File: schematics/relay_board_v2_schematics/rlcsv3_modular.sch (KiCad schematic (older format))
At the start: 37 parts, among them J1 Programming Header, P1 ACT_PWR, P3 ACTUATOR, Q1 MMBF170, Q2 MMBF170, SW1 SW_DIP_x04, U1 SPST_POWER_RELAY, U2 PIC16F1826-ISO, U3 dpdt_relay, U4 INA180A1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

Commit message: Add footprint to library
Signed-off-by: AIDAN HA <qbha@edu.uwaterloo.ca>
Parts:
- C1: footprint (none) -> Capacitors_SMD:C_0805_HandSoldering
- J1: footprint (none) -> rlcs:PinHeader_5x2.54_SMD_90deg_952-3198-1-ND
- R1, R13, R2, R3, R4: footprint (none) -> Resistors_SMD:R_0805_HandSoldering
- SW1: footprint (none) -> rlcs:DIP_SWITCH_4X2
- U2: footprint (none) -> rlcs:PIC16F1826-ISO
- U5: footprint (none) -> rlcs:2.54mm_pitch_1.3mm_hole_1x3_socket
- U6: footprint TO_SOT_Packages_SMD:SOT-23-5_HandSoldering -> rlcs:DCDC-Conv_IV1215SA
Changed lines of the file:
@@
 F 0 "U5" H 4938 1375 60  0000 L CNN
 F 1 "CONN_01x05" H 4938 1269 60  0000 L CNN
-F 2 "" H 4850 1600 60  0001 C CNN
+F 2 "rlcs:2.54mm_pitch_1.3mm_hole_1x3_socket" H 4850 1600 60  0001 C CNN
 F 3 "" H 4850 1600 60  0001 C CNN
 	1    4850 1500
@@
 F 0 "J1" H 1628 1226 50  0000 L CNN
 F 1 "Programming Header" H 1628 1135 50  0000 L CNN
-F 2 "" H 1600 1200 50  0001 C CNN
+F 2 "rlcs:PinHeader_5x2.54_SMD_90deg_952-3198-1-ND" H 1600 1200 50  0001 C CNN
 F 3 "~" H 1600 1200 50  0001 C CNN
 	1    1600 1200
@@
 F 0 "R1" H 2170 2496 50  0000 L CNN
 F 1 "10k" H 2170 2405 50  0000 L CNN
-F 2 "" V 2030 2450 50  0001 C CNN
+F 2 "Resistors_SMD:R_0805_HandSoldering" V 2030 2450 50  0001 C CNN
 F 3 "~" H 2100 2450 50  0001 C CNN
 	1    2100 2450
@@
 F 0 "SW1" H 1800 3267 50  0000 C CNN
 F 1 "SW_DIP_x04" H 1800 3176 50  0000 C CNN
-F 2 "" H 1800 2800 50  0001 C CNN
+F 2 "rlcs:DIP_SWITCH_4X2" H 1800 2800 50  0001 C CNN
 F 3 "~" H 1800 2800 50  0001 C CNN
 	1    1800 2800
@@
 F 0 "R3" H 3070 2496 50  0000 L CNN
 F 1 "10k" H 3070 2405 50  0000 L CNN
-F 2 "" V 2930 2450 50  0001 C CNN
+F 2 "Resistors_SMD:R_0805_HandSoldering" V 2930 2450 50  0001 C CNN
 F 3 "~" H 3000 2450 50  0001 C CNN
 	1    3000 2450
@@
 F 0 "R2" H 2670 2496 50  0000 L CNN
 F 1 "10k" H 2670 2405 50  0000 L CNN
-F 2 "" V 2530 2450 50  0001 C CNN
+F 2 "Resistors_SMD:R_0805_HandSoldering" V 2530 2450 50  0001 C CNN
 F 3 "~" H 2600 2450 50  0001 C CNN
 	1    2600 2450
@@
 F 0 "R4" H 3470 2496 50  0000 L CNN
 F 1 "10k" H 3470 2405 50  0000 L CNN
-F 2 "" V 3330 2450 50  0001 C CNN
+F 2 "Resistors_SMD:R_0805_HandSoldering" V 3330 2450 50  0001 C CNN
 F 3 "~" H 3400 2450 50  0001 C CNN
 	1    3400 2450
@@
 F 0 "R13" H 5130 2496 50  0000 L CNN
 F 1 "10K" H 5130 2405 50  0000 L CNN
-F 2 "" V 4990 2450 50  0001 C CNN
+F 2 "Resistors_SMD:R_0805_HandSoldering" V 4990 2450 50  0001 C CNN
 F 3 "~" H 5060 2450 50  0001 C CNN
 	1    5060 2450
@@
 F 0 "C1" V 7913 2546 50  0000 L CNN
 F 1 "22uF" V 7835 2455 50  0000 L CNN
-F 2 "" H 7758 2350 50  0001 C CNN
+F 2 "Capacitors_SMD:C_0805_HandSoldering" H 7758 2350 50  0001 C CNN
 F 3 "~" H 7720 2500 50  0001 C CNN
 	1    7720 2500
@@
 F 0 "U2" H 6200 3087 60  0000 C CNN
 F 1 "PIC16F1826-ISO" H 6200 2981 60  0000 C CNN
-F 2 "" H 6200 2950 60  0001 C CNN
+F 2 "rlcs:PIC16F1826-ISO" H 6200 2950 60  0001 C CNN
 F 3 "" H 6200 2950 60  0001 C CNN
 	1    6200 2500
@@
 F 0 "U6" H 9840 5100 50  0000 C CNN
 F 1 "INA180A1" H 9990 4700 50  0000 C CNN
-F 2 "TO_SOT_Packages_SMD:SOT-23-5_HandSoldering" H 9740 5000 50  0001 C CNN
+F 2 "rlcs:DCDC-Conv_IV1215SA" H 9740 5000 50  0001 C CNN
 F 3 "" H 9840 5100 50  0000 C CNN
 	1    9790 4900

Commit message: Add initial board layout
Signed-off-by: AIDAN HA <qbha@edu.uwaterloo.ca>
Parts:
- added U7: CONN_01x05, Connector_JST:JST_XH_S5B-XH-A-1_1x05_P2.50mm_Horizontal, symbol rlcsv3_modular-rescue:CONN_01x05
- C1, C2, C3: footprint Capacitors_SMD:C_0805_HandSoldering -> Capacitor_SMD:C_0805_2012Metric_Pad1.15x1.40mm_HandSolder
- D1, D2: footprint Diodes_THT:D_DO-35_SOD27_P7.62mm_Horizontal -> Diode_THT:D_DO-35_SOD27_P7.62mm_Horizontal
- F1: footprint custom:littlefuse_01000020Z -> rlcs:littlefuse_01000020Z
- P1: footprint Terminal_Blocks:TerminalBlock_Pheonix_MKDS1.5-2pol -> TerminalBlock_Phoenix:TerminalBlock_Phoenix_MKDS-1,5-2-5.08_1x02_P5.08mm_Horizontal
- P3: footprint Terminal_Blocks:TerminalBlock_Pheonix_MKDS1.5-6pol -> TerminalBlock_Phoenix:TerminalBlock_Phoenix_MKDS-1,5-6-5.08_1x06_P5.08mm_Horizontal
- Q1, Q2: footprint TO_SOT_Packages_SMD:SOT-23 -> Package_TO_SOT_SMD:SOT-23
- R1, R10, R11, R12, R13, R2, R3, R4, R5, R6, R7, R8, R9: footprint Resistors_SMD:R_0805_HandSoldering -> Resistor_SMD:R_0805_2012Metric_Pad1.15x1.40mm_HandSolder
- R14, R15: footprint Resistors_SMD:R_2512_HandSoldering -> Resistor_SMD:R_2512_6332Metric_Pad1.52x3.35mm_HandSolder
- U1: footprint custom:Relay_SPST_G5LE-1A -> rlcs:Relay_SPST_G5LE-1A
- U3: footprint custom:Relay_DPDT_RT424012F -> rlcs:Relay_DPDT_RT424012F
- U4: footprint TO_SOT_Packages_SMD:SOT-23-5_HandSoldering -> Package_TO_SOT_SMD:SOT-23-5_HandSoldering
- U5: footprint rlcs:2.54mm_pitch_1.3mm_hole_1x3_socket -> Connector_JST:JST_XH_S5B-XH-A-1_1x05_P2.50mm_Horizontal
- U6: footprint rlcs:DCDC-Conv_IV1215SA -> Package_TO_SOT_SMD:SOT-23-5_HandSoldering
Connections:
- net +12V: now also U5.1, U7.5; no longer U5.2
- net +5V: now also U5.2, U7.4; no longer U5.1
- net GND: now also U7.3
- net SCL: now also U5.4, U7.2; no longer U5.5
- net SDA: now also U5.5, U7.1; no longer U5.4
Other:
- moved on the sheet: U5

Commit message: Added traces
Signed-off-by: AIDAN HA <qbha@edu.uwaterloo.ca>
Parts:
- P3: footprint TerminalBlock_Phoenix:TerminalBlock_Phoenix_MKDS-1,5-6-5.08_1x06_P5.08mm_Horizontal -> TerminalBlock_Phoenix:TerminalBlock_Phoenix_MKDS-1,5-6_1x06_P5.00mm_Horizontal
- Q1, Q2: footprint Package_TO_SOT_SMD:SOT-23 -> Package_TO_SOT_SMD:SOT-23_Handsoldering
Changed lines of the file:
@@
 F 0 "Q1" H 4890 5225 50  0000 L CNN
 F 1 "MMBF170" H 4890 5150 50  0000 L CNN
-F 2 "Package_TO_SOT_SMD:SOT-23" H 4890 5075 50  0001 L CIN
+F 2 "Package_TO_SOT_SMD:SOT-23_Handsoldering" H 4890 5075 50  0001 L CIN
 F 3 "" H 4690 5150 50  0001 L CNN
 	1    4690 5150
@@
 F 0 "Q2" H 4890 7025 50  0000 L CNN
 F 1 "MMBF170" H 4890 6950 50  0000 L CNN
-F 2 "Package_TO_SOT_SMD:SOT-23" H 4890 6875 50  0001 L CIN
+F 2 "Package_TO_SOT_SMD:SOT-23_Handsoldering" H 4890 6875 50  0001 L CIN
 F 3 "" H 4690 6950 50  0001 L CNN
 	1    4690 6950
@@
 F 0 "P3" H 10600 2200 50  0000 C CNN
 F 1 "ACTUATOR" V 10700 1850 50  0000 C CNN
-F 2 "TerminalBlock_Phoenix:TerminalBlock_Phoenix_MKDS-1,5-6-5.08_1x06_P5.08mm_Horizontal" H 10600 1850 50  0001 C CNN
+F 2 "TerminalBlock_Phoenix:TerminalBlock_Phoenix_MKDS-1,5-6_1x06_P5.00mm_Horizontal" H 10600 1850 50  0001 C CNN
 F 3 "" H 10600 1850 50  0000 C CNN
 	1    10600 1850

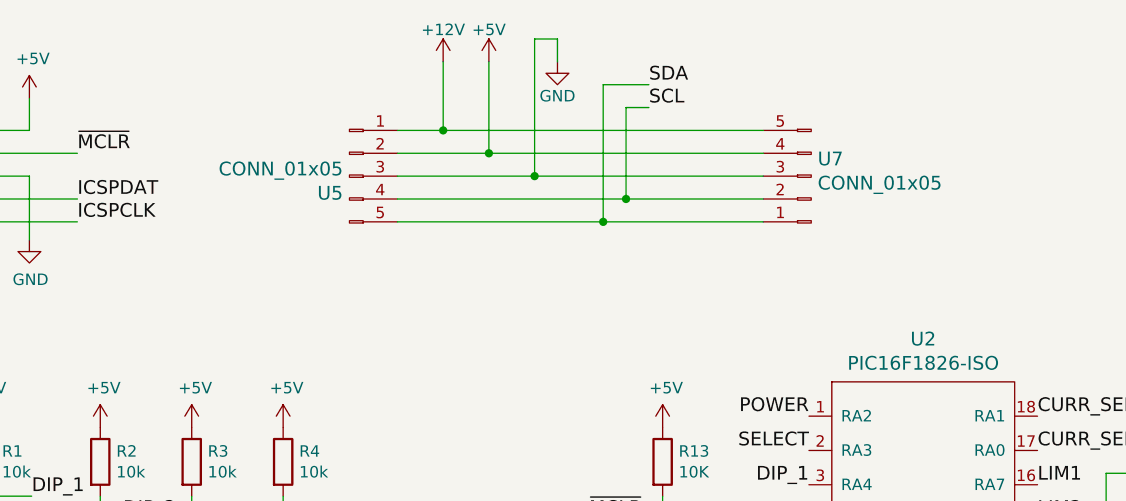
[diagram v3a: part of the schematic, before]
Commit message: Fix comments, add ground pour and DRC check changes
Signed-off-by: AIDAN HA <qbha@edu.uwaterloo.ca>
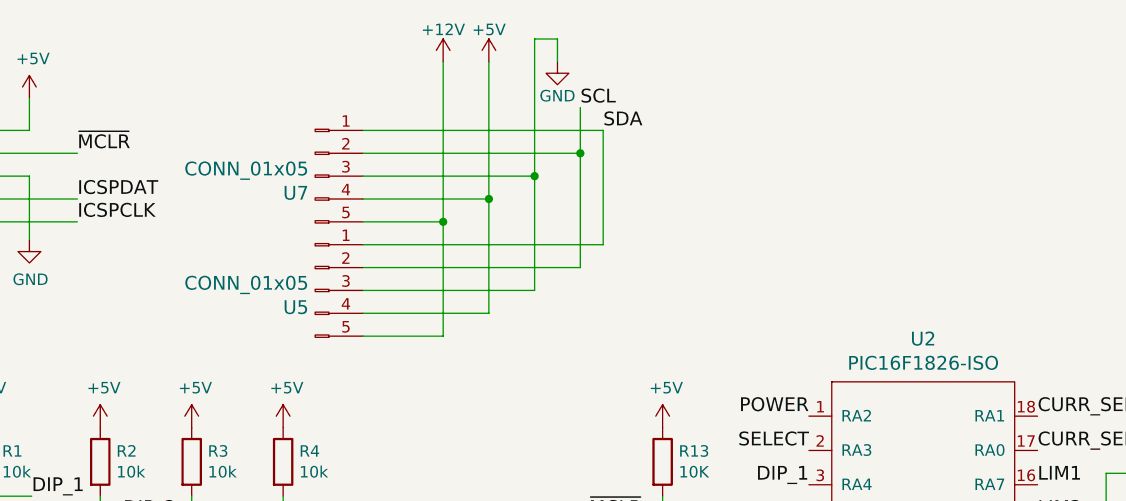
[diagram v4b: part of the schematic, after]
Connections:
- net +12V: now also U5.5; no longer U5.1
- net +5V: now also U5.4; no longer U5.2
- net SCL: now also U5.2; no longer U5.4
- net SDA: now also U5.1; no longer U5.5
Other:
- moved on the sheet: U5, U7
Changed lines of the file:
@@
-$EndComp
-$Comp
-L rlcsv3_modular-rescue:GND #PWR04
-U 1 1 5DD8888A
-P 4600 700
-F 0 "#PWR04" H 4600 450 50  0001 C CNN
-F 1 "GND" H 4600 550 50  0000 C CNN
-F 2 "" H 4600 700 50  0000 C CNN
-F 3 "" H 4600 700 50  0000 C CNN
-	1    4600 700
-	1    0    0    -1
-$EndComp
-$Comp
-L rlcsv3_modular-rescue:+12V #PWR03
-U 1 1 5DD80B39
-P 4100 700
-F 0 "#PWR03" H 4100 550 50  0001 C CNN
-F 1 "+12V" H 4100 840 50  0000 C CNN
-F 2 "" H 4100 700 50  0000 C CNN
-F 3 "" H 4100 700 50  0000 C CNN
-	1    4100 700
-	1    0    0    -1
 $EndComp
 $Comp
 L rlcsv3_modular-rescue:CONN_01x05 U5
 U 1 1 5DD7AFDF
-P 3750 1400
-F 0 "U5" H 3838 1275 60  0000 L CNN
-F 1 "CONN_01x05" H 3838 1169 60  0000 L CNN
-F 2 "Connector_JST:JST_XH_S5B-XH-A-1_1x05_P2.50mm_Horizontal" H 3750 1500 60  0001 C CNN
-F 3 "" H 3750 1500 60  0001 C CNN
-	1    3750 1400
+P 3600 1900
+F 0 "U5" H 3688 1775 60  0000 L CNN
+F 1 "CONN_01x05" H 3688 1669 60  0000 L CNN
+F 2 "Connector_JST:JST_XH_S5B-XH-A-1_1x05_P2.50mm_Horizontal" H 3600 2000 60  0001 C CNN
+F 3 "" H 3600 2000 60  0001 C CNN
+	1    3600 1900
 	-1   0    0    1
 $EndComp
@@
 	1    0    0    -1
 $EndComp
-Wire Wire Line
-	4100 700  4100 1000
-Wire Wire Line
-	3900 1200 4500 1200
-Wire Wire Line
-	4500 1200 4500 600
-Wire Wire Line
-	4500 600  4600 600
-Wire Wire Line
-	4600 600  4600 700
 Text Notes 1550 3490 0    60   ~ 0
 The dip switches are for physically setting\n a board "ID" or I2C address so that the software \nknows which board it's dealing with.
@@
 	7000 2850 6700 2850
 Connection ~ 7500 2500
-$Comp
-L rlcsv3_modular-rescue:CONN_01x05 U7
-U 1 1 5E36C206
-P 5650 1000
-F 0 "U7" H 5738 875 60  0000 L CNN
-F 1 "CONN_01x05" H 5738 769 60  0000 L CNN
-F 2 "Connector_JST:JST_XH_S5B-XH-A-1_1x05_P2.50mm_Horizontal" H 5650 1100 60  0001 C CNN
-F 3 "" H 5650 1100 60  0001 C CNN
-	1    5650 1000
-	1    0    0    -1
-$EndComp
-Text Label 5000 900  0    60   ~ 0
+Text Label 4700 900  0    60   ~ 0
 SCL
-Text Label 5000 800  0    60   ~ 0
+Text Label 4800 1000 0    60   ~ 0
 SDA
-Wire Wire Line
-	4900 1300 4900 900
-Wire Wire Line
-	4900 900  5000 900
-Wire Wire Line
-	3900 1300 4900 1300
-Wire Wire Line
-	5000 800  4800 800
-Wire Wire Line
-	4800 800  4800 1400
-Wire Wire Line
-	3900 1400 4800 1400
-Wire Wire Line
-	4500 1200 5500 1200
-Connection ~ 4500 1200
-Wire Wire Line
-	4900 1300 5500 1300
-Connection ~ 4900 1300
-Wire Wire Line
-	4800 1400 5500 1400
-Connection ~ 4800 1400
+$Comp
+L rlcsv3_modular-rescue:+12V #PWR03
+U 1 1 5DD80B39
+P 4100 700
+F 0 "#PWR03" H 4100 550 50  0001 C CNN
+F 1 "+12V" H 4100 840 50  0000 C CNN
+F 2 "" H 4100 700 50  0000 C CNN
+F 3 "" H 4100 700 50  0000 C CNN
+	1    4100 700
+	1    0    0    -1
+$EndComp
 $Comp
 L rlcsv3_modular-rescue:+5V #PWR02
@@
 $EndComp
 Wire Wire Line
-	3900 1000 4100 1000
-Wire Wire Line
-	3900 1100 4300 1100
-Connection ~ 4100 1000
-Wire Wire Line
-	4100 1000 5500 1000
-Wire Wire Line
-	4300 700  4300 1100
-Connection ~ 4300 1100
-Wire Wire Line
-	4300 1100 5500 1100
+	4600 600  4600 700
+Wire Wire Line
+	4500 600  4600 600
+$Comp
+L rlcsv3_modular-rescue:GND #PWR04
+U 1 1 5DD8888A
+P 4600 700
+F 0 "#PWR04" H 4600 450 50  0001 C CNN
+F 1 "GND" H 4600 550 50  0000 C CNN
+F 2 "" H 4600 700 50  0000 C CNN
+F 3 "" H 4600 700 50  0000 C CNN
+	1    4600 700
+	1    0    0    -1
+$EndComp
+$Comp
+L rlcsv3_modular-rescue:CONN_01x05 U7
+U 1 1 5E36C206
+P 3600 1400
+F 0 "U7" H 3688 1275 60  0000 L CNN
+F 1 "CONN_01x05" H 3688 1169 60  0000 L CNN
+F 2 "Connector_JST:JST_XH_S5B-XH-A-1_1x05_P2.50mm_Horizontal" H 3600 1500 60  0001 C CNN
+F 3 "" H 3600 1500 60  0001 C CNN
+	1    3600 1400
+	-1   0    0    1
+$EndComp
+Wire Wire Line
+	3750 1400 4100 1400
+Wire Wire Line
+	4100 1400 4100 700
+Wire Wire Line
+	4300 700  4300 1300
+Wire Wire Line
+	4300 1300 3750 1300
+Wire Wire Line
+	3750 1200 4500 1200
+Wire Wire Line
+	4500 1200 4500 600
+Wire Wire Line
+	3750 1100 4700 1100
+Wire Wire Line
+	4700 1100 4700 900
+Wire Wire Line
+	3750 1000 4800 1000
+Wire Wire Line
+	4100 1400 4100 1900
+Wire Wire Line
+	4100 1900 3750 1900
+Connection ~ 4100 1400
+Wire Wire Line
+	4300 1300 4300 1800
+Wire Wire Line
+	4300 1800 3750 1800
+Connection ~ 4300 1300
+Wire Wire Line
+	4500 1200 4500 1700
+Wire Wire Line
+	4500 1700 3750 1700
+Connection ~ 4500 1200
+Wire Wire Line
+	4700 1100 4700 1600
+Wire Wire Line
+	4700 1600 3750 1600
+Connection ~ 4700 1100
+Wire Wire Line
+	4800 1000 4800 1500
+Wire Wire Line
+	4800 1500 3750 1500
 $EndSCHEMATC

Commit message: Add round 3 of changes
Signed-off-by: AIDAN HA <qbha@edu.uwaterloo.ca>
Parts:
- added P2: ACT_PWR, TerminalBlock_Phoenix:TerminalBlock_Phoenix_MKDS-1,5-2-5.08_1x02_P5.08mm_Horizontal, symbol rlcsv3_modular-rescue:CONN_01X02
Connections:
- net GND: now also P2.1 (P1)
- net at F1.1, P1.2 (P2): now also P2.2 (P2)
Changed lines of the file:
@@
 Connection ~ 6140 4750
 Wire Wire Line
-	6790 4650 6790 4350
+	6790 4650 6790 4500
 Wire Wire Line
 	6790 4350 6690 4350
@@
 Wire Wire Line
 	4800 1500 3750 1500
+$Comp
+L rlcsv3_modular-rescue:CONN_01X02 P2
+U 1 1 5E6558C8
+P 7540 4700
+F 0 "P2" H 7540 4850 50  0000 C CNN
+F 1 "ACT_PWR" V 7640 4700 50  0000 C CNN
+F 2 "TerminalBlock_Phoenix:TerminalBlock_Phoenix_MKDS-1,5-2-5.08_1x02_P5.08mm_Horizontal" H 7540 4700 50  0001 C CNN
+F 3 "" H 7540 4700 50  0000 C CNN
+	1    7540 4700
+	1    0    0    -1
+$EndComp
+Wire Wire Line
+	6790 4500 7340 4500
+Wire Wire Line
+	7340 4500 7340 4650
+Connection ~ 6790 4500
+Wire Wire Line
+	6790 4500 6790 4350
+Wire Wire Line
+	6790 4750 6790 4910
+Wire Wire Line
+	6790 4910 7340 4910
+Wire Wire Line
+	7340 4910 7340 4750
+Connection ~ 6790 4750
 $EndSCHEMATC

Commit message: Add final silkscreen changes
Signed-off-by: AIDAN HA <qbha@edu.uwaterloo.ca>
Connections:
- net +5V: now also J1.4 (Pin_4); no longer J1.5 (Pin_5)
- net ~MCLR: now also J1.5 (Pin_5); no longer J1.4 (Pin_4)
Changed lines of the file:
@@
 L power:+5V #PWR?
 U 1 1 5DFBEBFA
-P 2290 860
+P 2290 960
 AR Path="/5DCB71CA/5DFBEBFA" Ref="#PWR?"  Part="1"
 AR Path="/5DFBEBFA" Ref="#PWR011"  Part="1"
-F 0 "#PWR011" H 2290 710 50  0001 C CNN
-F 1 "+5V" H 2305 1033 50  0000 C CNN
-F 2 "" H 2290 860 50  0001 C CNN
-F 3 "" H 2290 860 50  0001 C CNN
-	1    2290 860
+F 0 "#PWR011" H 2290 810 50  0001 C CNN
+F 1 "+5V" H 2305 1133 50  0000 C CNN
+F 2 "" H 2290 960 50  0001 C CNN
+F 3 "" H 2290 960 50  0001 C CNN
+	1    2290 960
 	1    0    0    -1
 $EndComp
-Text Label 2500 1100 0    60   ~ 0
+Text Label 2500 1000 0    60   ~ 0
 ~MCLR
 Wire Wire Line
-	2290 860  2290 1000
+	2290 960  2290 1100
 Wire Wire Line
-	2290 1000 1800 1000
+	2290 1100 1800 1100
 Wire Wire Line
-	1800 1100 2500 1100
+	1800 1000 2500 1000
 $Comp
 L power:GND #PWR?

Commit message: Fix SilkScreen and add Gerbers
Signed-off-by: AIDAN HA <qbha@edu.uwaterloo.ca>
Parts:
- added D3: D, LED_SMD:LED_1206_3216Metric_Pad1.42x1.75mm_HandSolder, symbol Device:D
- added R16: R, Resistor_SMD:R_0805_2012Metric_Pad1.15x1.40mm_HandSolder, symbol Device:R
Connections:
- net GND: now also R16.2
- net at U2.11 (RB5): now also D3.2 (A)
- new net: D3.1 (K), R16.1
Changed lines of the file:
@@
 	7340 4910 7340 4750
 Connection ~ 6790 4750
+$Comp
+L Device:R R16
+U 1 1 5E4CEE38
+P 7200 3950
+F 0 "R16" H 7270 3996 50  0000 L CNN
+F 1 "R" H 7270 3905 50  0000 L CNN
+F 2 "Resistor_SMD:R_0805_2012Metric_Pad1.15x1.40mm_HandSolder" V 7130 3950 50  0001 C CNN
+F 3 "~" H 7200 3950 50  0001 C CNN
+	1    7200 3950
+	1    0    0    -1
+$EndComp
+$Comp
+L Device:D D3
+U 1 1 5E4CF542
+P 7200 3550
+F 0 "D3" V 7246 3471 50  0000 R CNN
+F 1 "D" V 7155 3471 50  0000 R CNN
+F 2 "LED_SMD:LED_1206_3216Metric_Pad1.42x1.75mm_HandSolder" H 7200 3550 50  0001 C CNN
+F 3 "~" H 7200 3550 50  0001 C CNN
+	1    7200 3550
+	0    -1   -1   0
+$EndComp
+$Comp
+L power:GND #PWR034
+U 1 1 5E4D2187
+P 7200 4200
+F 0 "#PWR034" H 7200 3950 50  0001 C CNN
+F 1 "GND" H 7205 4027 50  0000 C CNN
+F 2 "" H 7200 4200 50  0001 C CNN
+F 3 "" H 7200 4200 50  0001 C CNN
+	1    7200 4200
+	1    0    0    -1
+$EndComp
+Wire Wire Line
+	7200 4100 7200 4200
+Wire Wire Line
+	7200 3300 6700 3300
+Wire Wire Line
+	7200 3400 7200 3300
+Wire Wire Line
+	7200 3800 7200 3700
 $EndSCHEMATC

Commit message: Add current rating to relay board fuse
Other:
- note added: "Fuse: \nBlowout Current = 20 A\nType = Glass Cartridge\nSize = 5mm x 20 mm"
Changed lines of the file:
@@
 EESchema Schematic File Version 4
+LIBS:rlcsv3_modular-cache
 EELAYER 30 0
 EELAYER END
@@
 Wire Wire Line
 	7200 3800 7200 3700
+Text Notes 6500 5300 0    60   ~ 0
+Fuse: \nBlowout Current = 20 A\nType = Glass Cartridge\nSize = 5mm x 20 mm
 $EndSCHEMATC
